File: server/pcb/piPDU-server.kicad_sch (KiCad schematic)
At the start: 22 parts, among them J1 Raspberry_Pi_2_3, U0 ACS712, U1 ACS712, U10 ACS712, U11 ACS712, U12 ACS712, U13 ACS712, U14 ACS712, U15 ACS712, U2 ACS712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

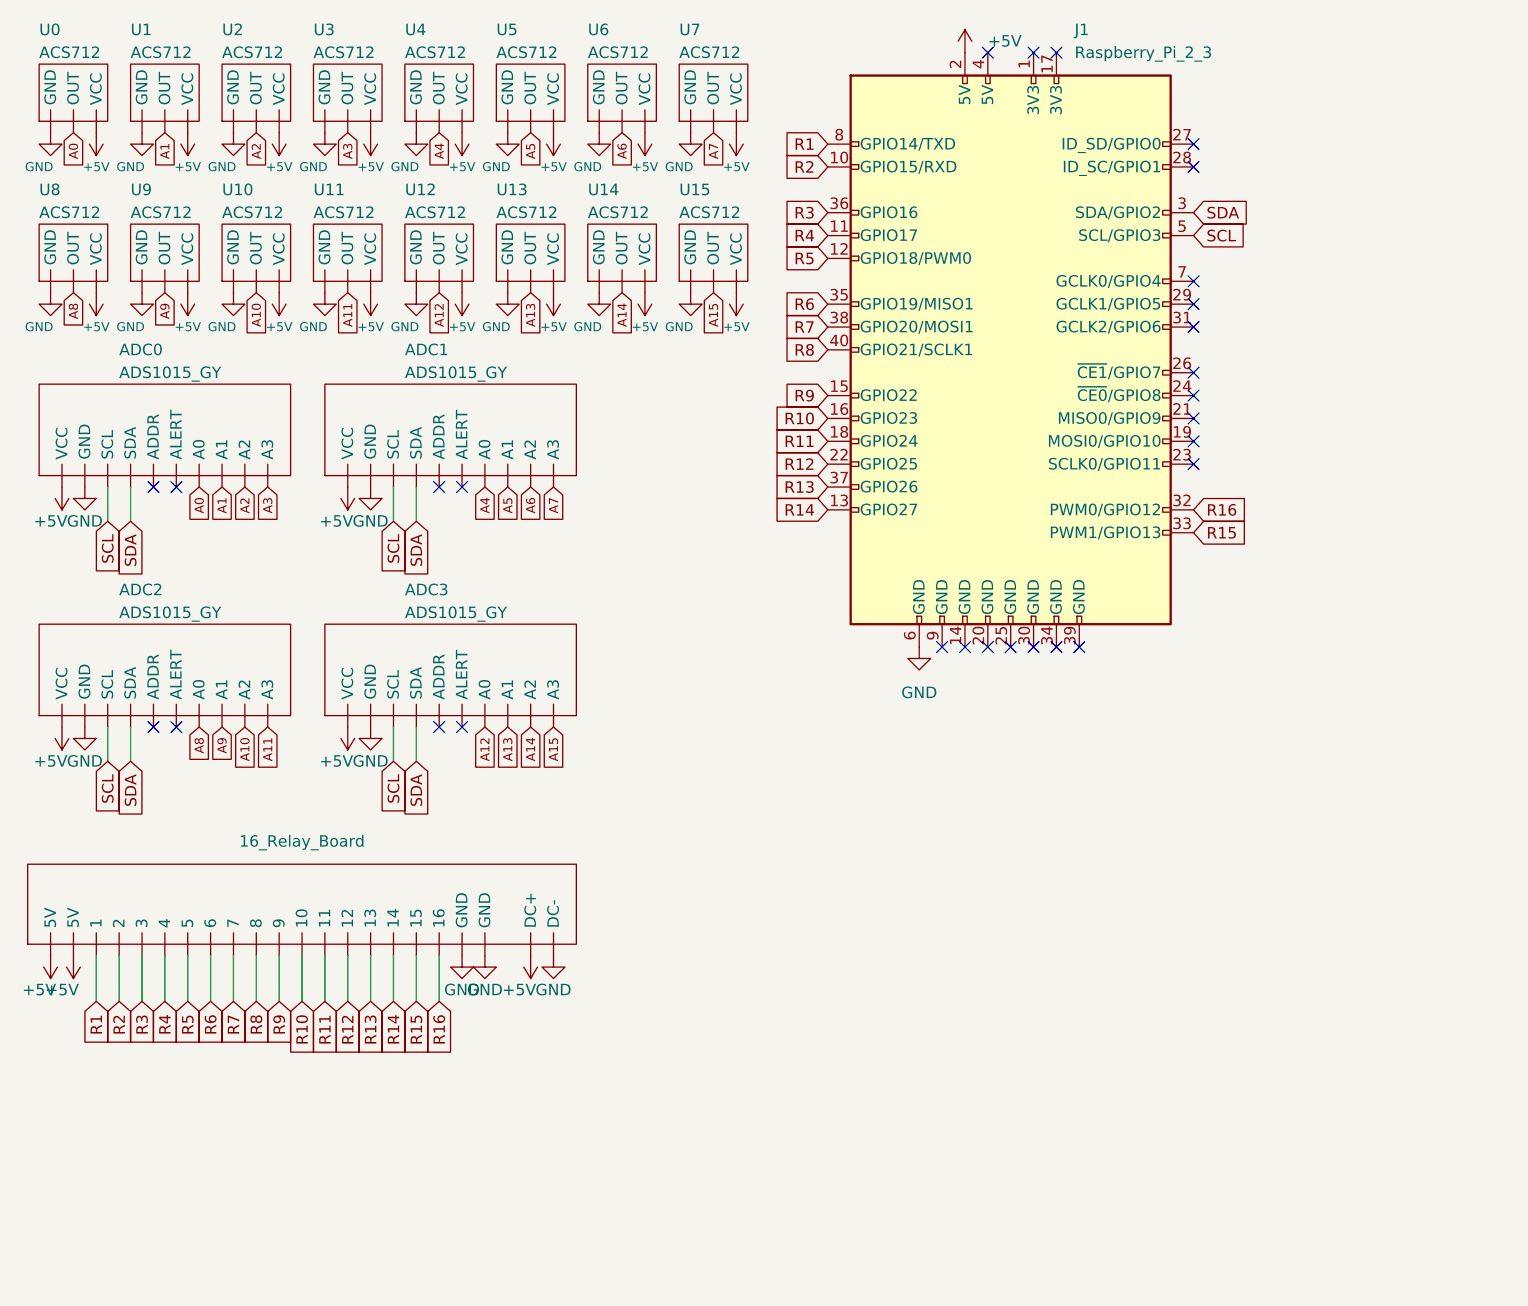
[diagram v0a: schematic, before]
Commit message: Update server schematic to use the Arduino Mega as I2C expander and remove the PCB design
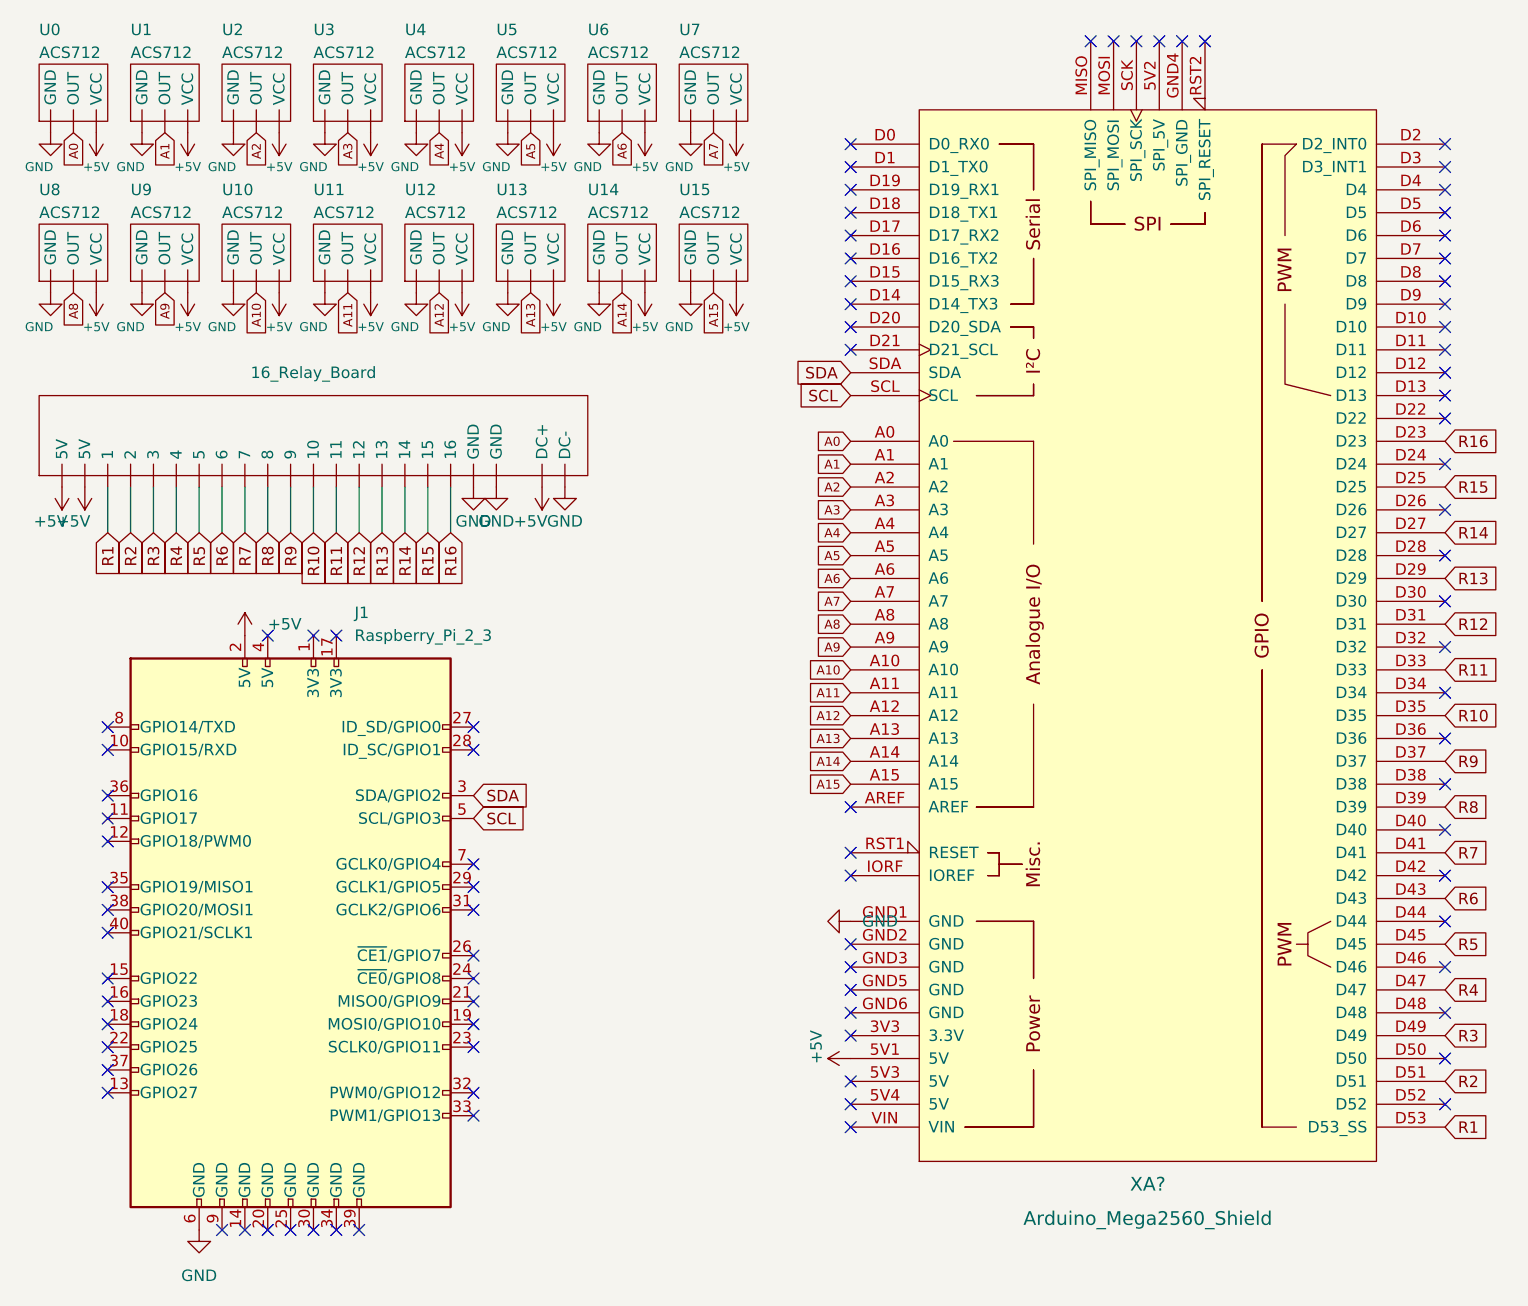
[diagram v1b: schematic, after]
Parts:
- removed ADC0, ADC1, ADC2, ADC3: ADS1015_GY, Custom:ADS1015 GY, symbol Custom:ADS1015_GY
- added XA?: Arduino_Mega2560_Shield, Arduino_Library:Arduino_Mega2560_Shield, symbol arduino:Arduino_Mega2560_Shield
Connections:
- net +5V: now also XA?.5V1 (5V)
- net A0: now also XA?.A0
- net A1: now also XA?.A1
- net A10: now also XA?.A10
- net A11: now also XA?.A11
- net A12: now also XA?.A12
- net A13: now also XA?.A13
- net A14: now also XA?.A14
- net A15: now also XA?.A15
- net A2: now also XA?.A2
- net A3: now also XA?.A3
- net A4: now also XA?.A4
- net A5: now also XA?.A5
- net A6: now also XA?.A6
- net A7: now also XA?.A7
- net A8: now also XA?.A8
- net A9: now also XA?.A9
- net GND: now also XA?.GND1 (GND)
- net R1: now also XA?.D53 (D53_SS); no longer J1.8 (GPIO14/TXD)
- net R10: now also XA?.D35; no longer J1.16 (GPIO23)
- net R11: now also XA?.D33; no longer J1.18 (GPIO24)
- net R12: now also XA?.D31; no longer J1.22 (GPIO25)
- net R13: now also XA?.D29; no longer J1.37 (GPIO26)
- net R14: now also XA?.D27; no longer J1.13 (GPIO27)
- net R15: now also XA?.D25; no longer J1.33 (PWM1/GPIO13)
- net R16: now also XA?.D23; no longer J1.32 (PWM0/GPIO12)
- net R2: now also XA?.D51; no longer J1.10 (GPIO15/RXD)
- net R3: now also XA?.D49; no longer J1.36 (GPIO16)
- net R4: now also XA?.D47; no longer J1.11 (GPIO17)
- net R5: now also XA?.D45; no longer J1.12 (GPIO18/PWM0)
- net R6: now also XA?.D43; no longer J1.35 (GPIO19/MISO1)
- net R7: now also XA?.D41; no longer J1.38 (GPIO20/MOSI1)
- net R8: now also XA?.D39; no longer J1.40 (GPIO21/SCLK1)
- net R9: now also XA?.D37; no longer J1.15 (GPIO22)
- net SCL: now also XA?.SCL
- net SDA: now also XA?.SDA
- no-connect marks 28 -> 91
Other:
- moved on the sheet: J1
